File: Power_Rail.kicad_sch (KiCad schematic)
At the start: 19 parts

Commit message: Schematic finish & ERC
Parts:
- gave numbers to parts that had none: 19

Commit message: Footprint Update
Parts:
- C14, C15, C16, C17, C18, C19: footprint (none) -> Capacitor_SMD:C_0402_1005Metric_Pad0.74x0.62mm_HandSolder
- D5, D6: footprint (none) -> LED_SMD:LED_0603_1608Metric_Pad1.05x0.95mm_HandSolder
- R16, R17, R18, R19, R20: footprint (none) -> Resistor_SMD:R_0402_1005Metric_Pad0.72x0.64mm_HandSolder
- TP1, TP2: footprint (none) -> TestPoint:TestPoint_Pad_D2.5mm
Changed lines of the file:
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@@
 			)
 		)
-		(property "Footprint" ""
+		(property "Footprint" "Capacitor_SMD:C_0402_1005Metric_Pad0.74x0.62mm_HandSolder"
 			(at 106.9848 54.61 0)
 			(effects
@@
 			)
 		)
-		(property "Footprint" ""
+		(property "Footprint" "Resistor_SMD:R_0402_1005Metric_Pad0.72x0.64mm_HandSolder"
 			(at 184.658 31.75 90)
 			(effects
@@
 			)
 		)
-		(property "Footprint" ""
+		(property "Footprint" "LED_SMD:LED_0603_1608Metric_Pad1.05x0.95mm_HandSolder"
 			(at 201.93 40.64 0)
 			(effects
@@
 			)
 		)
-		(property "Footprint" ""
+		(property "Footprint" "Capacitor_SMD:C_0402_1005Metric_Pad0.74x0.62mm_HandSolder"
 			(at 30.7848 52.07 0)
 			(effects
@@
 			)
 		)
-		(property "Footprint" ""
+		(property "Footprint" "Resistor_SMD:R_0402_1005Metric_Pad0.72x0.64mm_HandSolder"
 			(at 124.968 48.26 90)
 			(effects
@@
 			)
 		)
-		(property "Footprint" ""
+		(property "Footprint" "Capacitor_SMD:C_0402_1005Metric_Pad0.74x0.62mm_HandSolder"
 			(at 91.1352 52.07 0)
 			(effects
@@
 			)
 		)
-		(property "Footprint" ""
+		(property "Footprint" "Resistor_SMD:R_0402_1005Metric_Pad0.72x0.64mm_HandSolder"
 			(at 124.968 58.42 90)
 			(effects
@@
 			)
 		)
-		(property "Footprint" ""
+		(property "Footprint" "Resistor_SMD:R_0402_1005Metric_Pad0.72x0.64mm_HandSolder"
 			(at 203.708 31.75 90)
 			(effects
@@
 			)
 		)
-		(property "Footprint" ""
+		(property "Footprint" "TestPoint:TestPoint_Pad_D2.5mm"
 			(at 34.29 43.18 0)
 			(effects
@@
 			)
 		)
-		(property "Footprint" ""
+		(property "Footprint" "Capacitor_SMD:C_0402_1005Metric_Pad0.74x0.62mm_HandSolder"
 			(at 103.8352 54.61 0)
 			(effects
@@
 			)
 		)
-		(property "Footprint" ""
+		(property "Footprint" "Capacitor_SMD:C_0402_1005Metric_Pad0.74x0.62mm_HandSolder"
 			(at 27.6352 52.07 0)
 			(effects
@@
 			)
 		)
-		(property "Footprint" ""
+		(property "Footprint" "LED_SMD:LED_0603_1608Metric_Pad1.05x0.95mm_HandSolder"
 			(at 182.88 40.64 0)
 			(effects
@@
 			)
 		)
-		(property "Footprint" ""
+		(property "Footprint" "Capacitor_SMD:C_0402_1005Metric_Pad0.74x0.62mm_HandSolder"
 			(at 67.31 28.2448 0)
 			(effects
@@
 			)
 		)
-		(property "Footprint" ""
+		(property "Footprint" "TestPoint:TestPoint_Pad_D2.5mm"
 			(at 128.27 40.64 0)
 			(effects
@@
 			)
 		)
-		(property "Footprint" ""
+		(property "Footprint" "Resistor_SMD:R_0402_1005Metric_Pad0.72x0.64mm_HandSolder"
 			(at 91.948 64.77 90)
 			(effects

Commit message: Layout Update
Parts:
- removed J4: 43045-0200, KSZ_KiCad_Footprint_Library:43045-02YY, symbol KSZ_KiCad_Symbol_Library:43045-0200
- removed TP1: 12V, TestPoint:TestPoint_Pad_D2.5mm, symbol Connector:TestPoint
- removed TP2: 3.3V, TestPoint:TestPoint_Pad_D2.5mm, symbol Connector:TestPoint
- added J4: Conn_01x02_Socket, Connector_JST:JST_PH_S2B-PH-K_1x02_P2.00mm_Horizontal, symbol Connector:Conn_01x02_Socket
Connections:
- net +12V: now also J4.1 (Pin_1)
- net GND: now also J4.2 (Pin_2)

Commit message: Layout Update
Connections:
- net +12V: now also J4.2 (Pin_2); no longer J4.1 (Pin_1)
- net GND: now also J4.1 (Pin_1); no longer J4.2 (Pin_2)
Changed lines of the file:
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@@
 	(symbol
 		(lib_id "Connector:Conn_01x02_Socket")
-		(at 157.48 24.13 0)
+		(at 157.48 26.67 0)
+		(mirror x)
 		(unit 1)
 		(exclude_from_sim no)
@@
 		(dnp no)
 		(property "Reference" "J4"
-			(at 158.75 24.1299 0)
+			(at 158.75 26.6701 0)
 			(effects
 				(font
@@
 		)
 		(property "Value" "Conn_01x02_Socket"
-			(at 158.75 26.6699 0)
+			(at 158.75 24.1301 0)
 			(effects
 				(font
@@
 		)
 		(property "Footprint" "Connector_JST:JST_PH_S2B-PH-K_1x02_P2.00mm_Horizontal"
-			(at 157.48 24.13 0)
+			(at 157.48 26.67 0)
 			(effects
 				(font
@@
 		)
 		(property "Datasheet" "~"
-			(at 157.48 24.13 0)
+			(at 157.48 26.67 0)
 			(effects
 				(font
@@
 		)
 		(property "Description" "Generic connector, single row, 01x02, script generated"
-			(at 157.48 24.13 0)
+			(at 157.48 26.67 0)
 			(effects
 				(font

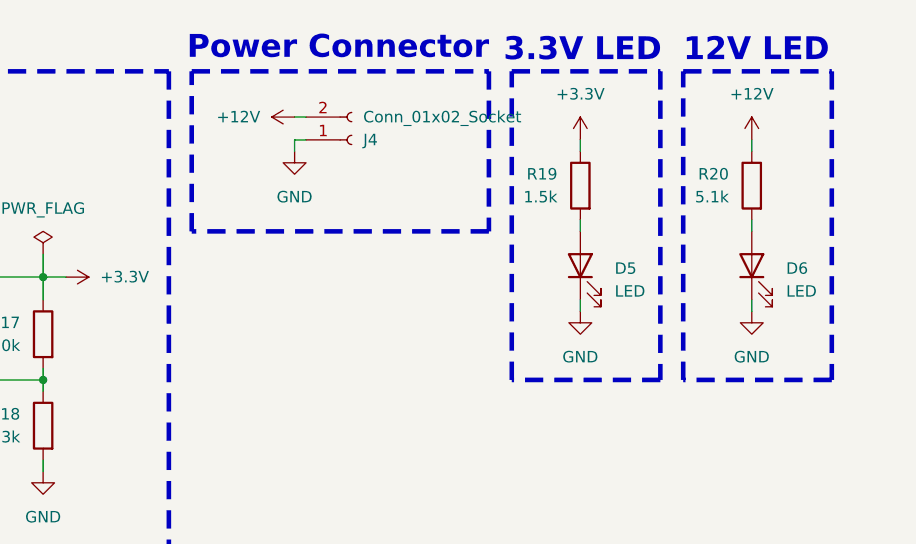
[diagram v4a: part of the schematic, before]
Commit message: Schematic check, Text adjustment & QoL changes
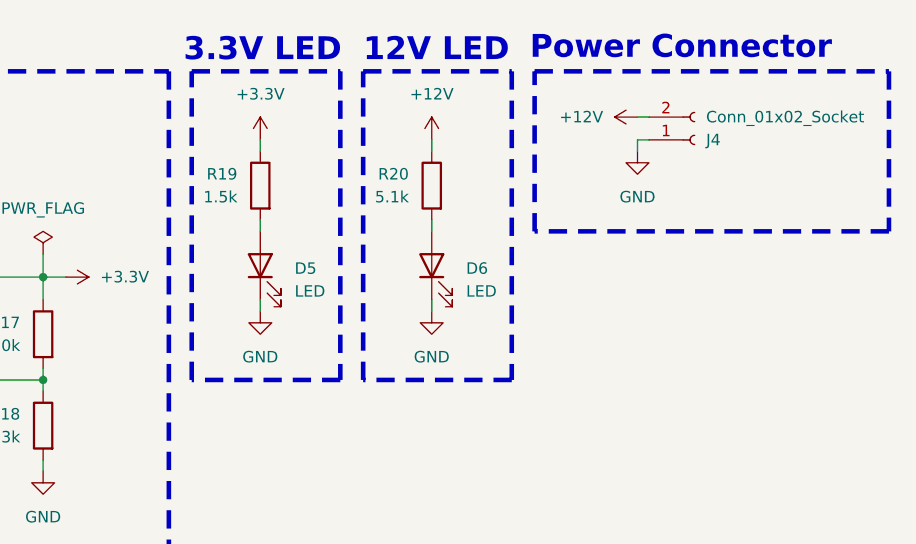
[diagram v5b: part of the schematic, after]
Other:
- moved on the sheet: D5, D6, J4, R19, R20

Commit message: Constrains & Check
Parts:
- C14, C15, C16, C17, C18, C19: footprint Capacitor_SMD:C_0402_1005Metric_Pad0.74x0.62mm_HandSolder -> Capacitor_SMD:C_0603_1608Metric_Pad1.08x0.95mm_HandSolder
- R16, R17, R18: footprint Resistor_SMD:R_0402_1005Metric_Pad0.72x0.64mm_HandSolder -> Resistor_SMD:R_0603_1608Metric_Pad0.98x0.95mm_HandSolder
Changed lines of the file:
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@@
 			)
 		)
-		(property "Footprint" "Capacitor_SMD:C_0402_1005Metric_Pad0.74x0.62mm_HandSolder"
+		(property "Footprint" "Capacitor_SMD:C_0603_1608Metric_Pad1.08x0.95mm_HandSolder"
 			(at 106.9848 54.61 0)
 			(effects
@@
 			)
 		)
-		(property "Footprint" "Capacitor_SMD:C_0402_1005Metric_Pad0.74x0.62mm_HandSolder"
+		(property "Footprint" "Capacitor_SMD:C_0603_1608Metric_Pad1.08x0.95mm_HandSolder"
 			(at 30.7848 52.07 0)
 			(effects
@@
 			)
 		)
-		(property "Footprint" "Resistor_SMD:R_0402_1005Metric_Pad0.72x0.64mm_HandSolder"
+		(property "Footprint" "Resistor_SMD:R_0603_1608Metric_Pad0.98x0.95mm_HandSolder"
 			(at 124.968 48.26 90)
 			(effects
@@
 			)
 		)
-		(property "Footprint" "Capacitor_SMD:C_0402_1005Metric_Pad0.74x0.62mm_HandSolder"
+		(property "Footprint" "Capacitor_SMD:C_0603_1608Metric_Pad1.08x0.95mm_HandSolder"
 			(at 91.1352 52.07 0)
 			(effects
@@
 			)
 		)
-		(property "Footprint" "Resistor_SMD:R_0402_1005Metric_Pad0.72x0.64mm_HandSolder"
+		(property "Footprint" "Resistor_SMD:R_0603_1608Metric_Pad0.98x0.95mm_HandSolder"
 			(at 124.968 58.42 90)
 			(effects
@@
 			)
 		)
-		(property "Footprint" "Capacitor_SMD:C_0402_1005Metric_Pad0.74x0.62mm_HandSolder"
+		(property "Footprint" "Capacitor_SMD:C_0603_1608Metric_Pad1.08x0.95mm_HandSolder"
 			(at 103.8352 54.61 0)
 			(effects
@@
 			)
 		)
-		(property "Footprint" "Capacitor_SMD:C_0402_1005Metric_Pad0.74x0.62mm_HandSolder"
+		(property "Footprint" "Capacitor_SMD:C_0603_1608Metric_Pad1.08x0.95mm_HandSolder"
 			(at 27.6352 52.07 0)
 			(effects
@@
 			)
 		)
-		(property "Footprint" "Capacitor_SMD:C_0402_1005Metric_Pad0.74x0.62mm_HandSolder"
+		(property "Footprint" "Capacitor_SMD:C_0603_1608Metric_Pad1.08x0.95mm_HandSolder"
 			(at 67.31 28.2448 0)
 			(effects
@@
 			)
 		)
-		(property "Footprint" "Resistor_SMD:R_0402_1005Metric_Pad0.72x0.64mm_HandSolder"
+		(property "Footprint" "Resistor_SMD:R_0603_1608Metric_Pad0.98x0.95mm_HandSolder"
 			(at 91.948 64.77 90)
 			(effects
